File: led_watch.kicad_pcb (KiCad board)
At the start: 6 copper layers, 29 x 29 mm, 107 parts, among them U3 M0G3507QDGS32RQ1, Y2 TXC-7C

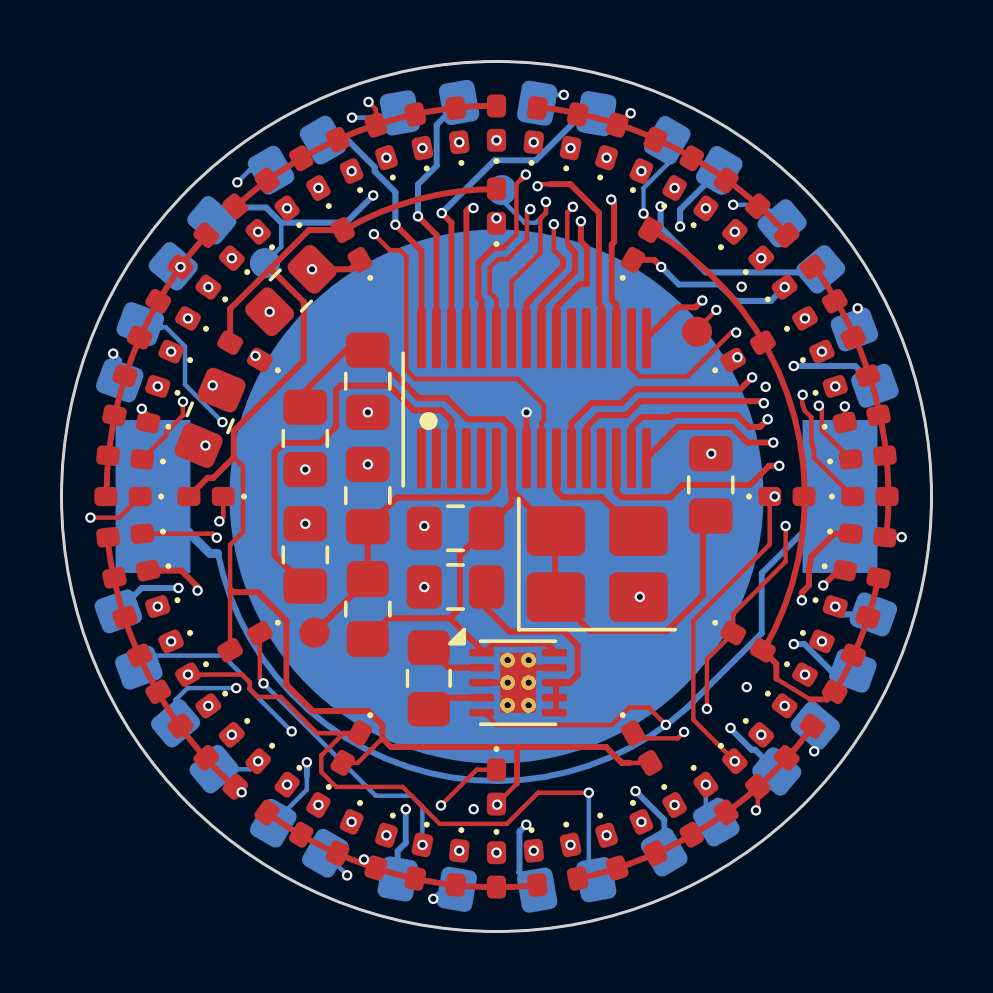
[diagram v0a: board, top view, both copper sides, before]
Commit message: 4 layers, removed regulator
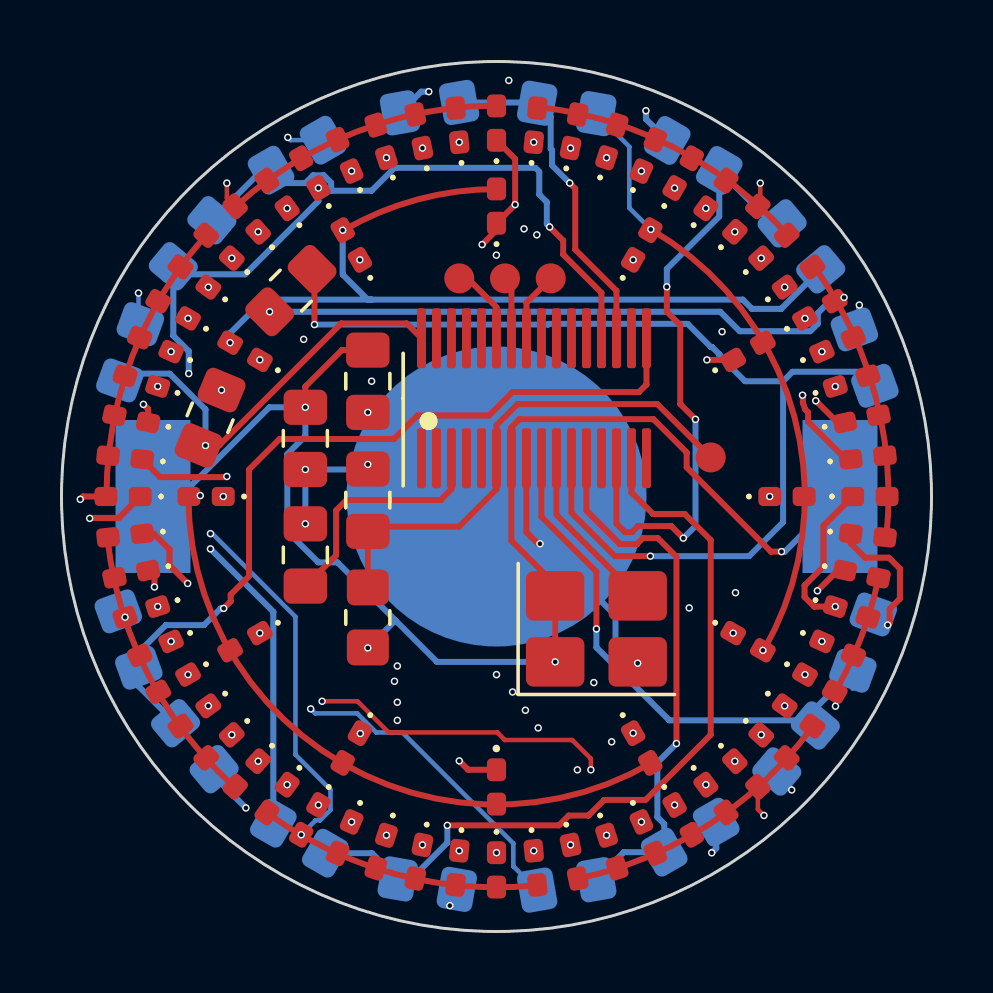
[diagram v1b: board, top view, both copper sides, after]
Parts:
- removed C1, C2: 10uF, Capacitor_SMD:C_0805_2012Metric_Pad1.18x1.45mm_HandSolder
- removed C3: 0.1uF, Capacitor_SMD:C_0805_2012Metric_Pad1.18x1.45mm_HandSolder
- removed L1: 2.2uH, Inductor_SMD:L_0805_2012Metric_Pad1.15x1.40mm_HandSolder
- removed PS1: TPS63031DSKR, Package_SON:WSON-10-1EP_2.5x2.5mm_P0.5mm_EP1.2x2mm_ThermalVias
- TP3, TP6: moved to F.Cu
- moved TP5 14.4 mm to (114.3, 50.9)
- moved TP6 9.54 mm to (109.0, 45.0)
- moved TP4 8.12 mm to (105.9, 45.0)
- moved TP3 2.94 mm to (107.4, 45.0)
- moved Y2 2.16 mm to (110.5, 56.6)
- moved R19 0.28 mm to (102.9, 56.3)
- moved C4 0.15 mm to (102.9, 52.3)
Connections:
- C7 pad 1: +3V3 -> +VBATT
- C8 pad 1: +3V3 -> +VBATT
- R10 pad 1: PA9 -> Net-(D33-A)
- R10 pad 2: Net-(D1-A) -> PA10
- R11 pad 1: PA16/SPI1_POCI -> PA25/SPI1_CS3
- R11 pad 2: Net-(D10-A) -> Net-(D13-K)
- R12 pad 1: PA17/SPI1_CLK -> Net-(D41-A)
- R12 pad 2: Net-(D17-A) -> PA25/SPI1_CS3
- R13 pad 1: PA18/SPI1_PICO/BSL_Invoke -> PA13/TFT_D/C
- R13 pad 2: Net-(D25-A) -> Net-(D14-K)
- R14 pad 1: PA25/SPI1_CS3 -> Net-(D49-A)
- R14 pad 2: Net-(D33-A) -> PA13/TFT_D/C
- R15 pad 1: PA24/TFT_RESET -> PA12
- R15 pad 2: Net-(D41-A) -> Net-(D15-K)
- R16 pad 1: PA23 -> Net-(D57-A)
- R16 pad 2: Net-(D49-A) -> PA12
- R17 pad 1: PA22 -> PA7
- R17 pad 2: Net-(D57-A) -> Net-(D16-K)
- R18 pad 1: PA21 -> Net-(D65-A)
- R18 pad 2: Net-(D65-A) -> PA7
- R19 pad 1: +3V3 -> +VBATT
- R2 pad 1: PA2 -> Net-(D1-A)
- R2 pad 2: Net-(D1-K) -> PA4
- R3 pad 1: PA5/HFXIN -> PA2
- R3 pad 2: Net-(D10-K) -> Net-(D1-K)
- R4 pad 1: PA8/SPI0_CS0 -> Net-(D10-A)
- R4 pad 2: Net-(D11-K) -> PA2
- R5 pad 1: PA10 -> PA5/HFXIN
- R5 pad 2: Net-(D12-K) -> Net-(D10-K)
- R6 pad 1: PA11/SPI0_SCK -> Net-(D17-A)
- R6 pad 2: Net-(D13-K) -> PA5/HFXIN
- R7 pad 1: PA12 -> PA8/SPI0_CS0
- R7 pad 2: Net-(D14-K) -> Net-(D11-K)
- R8 pad 1: PA13/TFT_D/C -> Net-(D25-A)
- R8 pad 2: Net-(D15-K) -> PA8/SPI0_CS0
- R9 pad 1: PA7 -> PA10
- R9 pad 2: Net-(D16-K) -> Net-(D12-K)
- U3 pad 7: +3V3 -> +VBATT
- Y2 pad 1: +3V3 -> +VBATT
- Y2 pad 4: +3V3 -> +VBATT
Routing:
- net Net-(D65-A): track 88.9 -> 30.9 mm, vias 2 -> 3
- net +3V3: track 36.6 -> 0.00 mm
- net PA11/SPI0_SCK: track 34.8 -> 0.00 mm, vias 2 -> 0
- net PA12: track 42.8 -> 11.5 mm, vias 2 -> 1
- net PA9: track 29.0 -> 0.00 mm, vias 2 -> 0
- net +VBATT: track 20.8 -> 48.4 mm, vias 1 -> 4
- net PA13/TFT_D/C: track 46.1 -> 19.1 mm, vias 2 -> 1
- net PA17/SPI1_CLK: track 26.9 -> 0.00 mm, vias 2 -> 0
- net PA16/SPI1_POCI: track 26.4 -> 0.00 mm, vias 2 -> 0
- net Net-(D33-A): track 24.8 -> 0.00 mm, vias 2 -> 1
- net PA4: track 12.3 -> 36.3 mm
- net PA18/SPI1_PICO/BSL_Invoke: track 24.5 -> 2.33 mm, vias 2 -> 0
- net Net-(D17-K): track 101.5 -> 81.0 mm, vias 9 -> 12
- net PA21: track 19.5 -> 0.00 mm, vias 2 -> 0
- net PA22: track 17.6 -> 0.00 mm, vias 2 -> 0
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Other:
- copper layers 6 -> 4

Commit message: remove half of resistors, routing cleanup
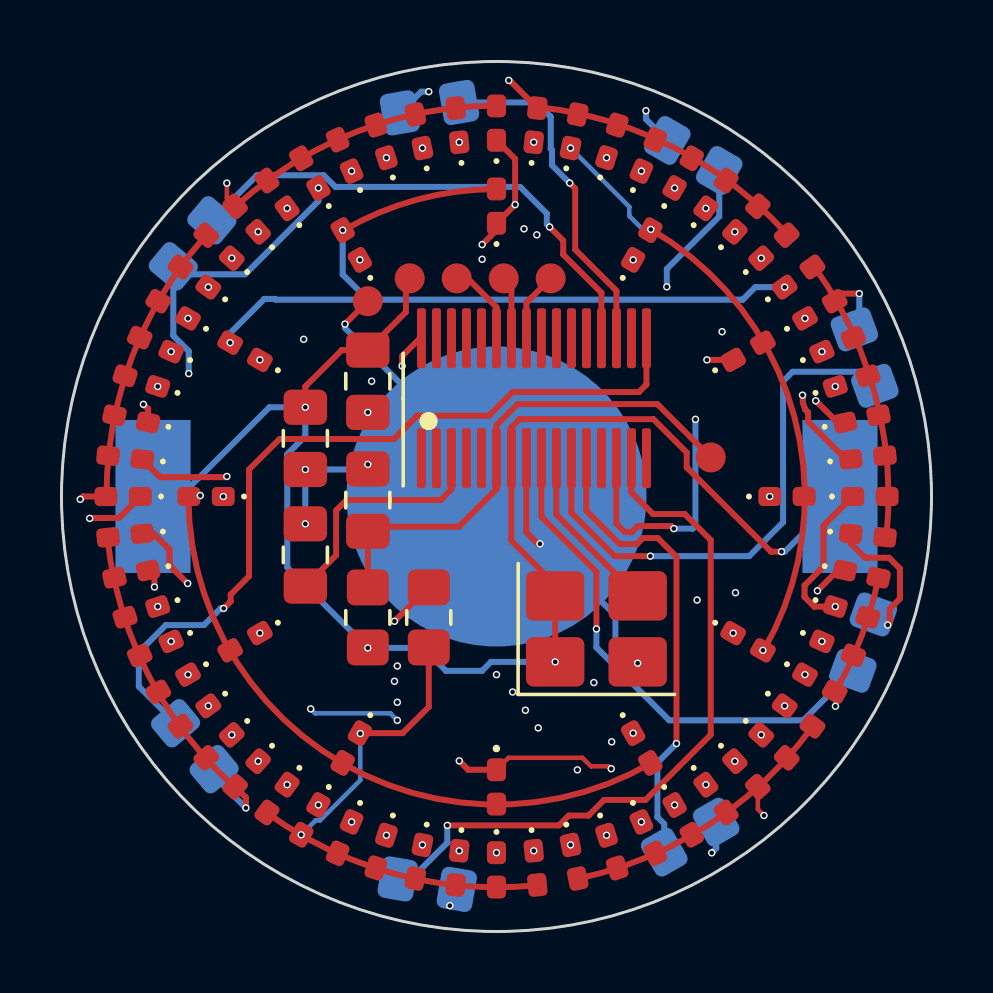
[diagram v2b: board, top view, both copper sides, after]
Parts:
- removed R10, R12, R14, R16, R18, R2, R4, R6, R8: 75, Resistor_SMD:R_0805_2012Metric_Pad1.20x1.40mm_HandSolder
- added TP1: TestPoint, TestPoint:TestPoint_Pad_D1.0mm, F.Cu at (104.3, 45.0)
- added TP2: TestPoint, TestPoint:TestPoint_Pad_D1.0mm, F.Cu at (102.9, 45.7)
- moved R11 9.87 mm to (104.9, 56.3), turned to -90 degrees
- moved TP4 0.08 mm to (105.8, 45.0)
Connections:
- D1 pad 1: Net-(D1-K) -> PA2
- D1 pad 2: Net-(D1-A) -> PA4
- D10 pad 1: Net-(D10-K) -> PA5/HFXIN
- D10 pad 2: Net-(D10-A) -> PA2
- D11 pad 1: Net-(D11-K) -> PA8/SPI0_CS0
- D11 pad 2: Net-(D10-A) -> PA2
- D12 pad 1: Net-(D12-K) -> PA10
- D12 pad 2: Net-(D10-A) -> PA2
- D13 pad 1: Net-(D13-K) -> PA25/SPI1_CS3
- D13 pad 2: Net-(D10-A) -> PA2
- D14 pad 1: Net-(D14-K) -> PA13/TFT_D/C
- D14 pad 2: Net-(D10-A) -> PA2
- D15 pad 1: Net-(D15-K) -> PA12
- D15 pad 2: Net-(D10-A) -> PA2
- D16 pad 1: Net-(D16-K) -> PA7
- D16 pad 2: Net-(D10-A) -> PA2
- D17 pad 1: Net-(D17-K) -> PA4
- D17 pad 2: Net-(D17-A) -> PA5/HFXIN
- D18 pad 1: Net-(D1-K) -> PA2
- D18 pad 2: Net-(D17-A) -> PA5/HFXIN
- D19 pad 1: Net-(D11-K) -> PA8/SPI0_CS0
- D19 pad 2: Net-(D17-A) -> PA5/HFXIN
- D2 pad 1: Net-(D10-K) -> PA5/HFXIN
- D2 pad 2: Net-(D1-A) -> PA4
- D20 pad 1: Net-(D12-K) -> PA10
- D20 pad 2: Net-(D17-A) -> PA5/HFXIN
- D21 pad 1: Net-(D13-K) -> PA25/SPI1_CS3
- D21 pad 2: Net-(D17-A) -> PA5/HFXIN
- D22 pad 1: Net-(D14-K) -> PA13/TFT_D/C
- D22 pad 2: Net-(D17-A) -> PA5/HFXIN
- D23 pad 1: Net-(D15-K) -> PA12
- D23 pad 2: Net-(D17-A) -> PA5/HFXIN
- D24 pad 1: Net-(D16-K) -> PA7
- D24 pad 2: Net-(D17-A) -> PA5/HFXIN
- D25 pad 1: Net-(D17-K) -> PA4
- D25 pad 2: Net-(D25-A) -> PA8/SPI0_CS0
- D26 pad 1: Net-(D1-K) -> PA2
- D26 pad 2: Net-(D25-A) -> PA8/SPI0_CS0
- D27 pad 1: Net-(D10-K) -> PA5/HFXIN
- D27 pad 2: Net-(D25-A) -> PA8/SPI0_CS0
- D28 pad 1: Net-(D12-K) -> PA10
- D28 pad 2: Net-(D25-A) -> PA8/SPI0_CS0
- D29 pad 1: Net-(D13-K) -> PA25/SPI1_CS3
- D29 pad 2: Net-(D25-A) -> PA8/SPI0_CS0
- D3 pad 1: Net-(D11-K) -> PA8/SPI0_CS0
- D3 pad 2: Net-(D1-A) -> PA4
- D30 pad 1: Net-(D14-K) -> PA13/TFT_D/C
- D30 pad 2: Net-(D25-A) -> PA8/SPI0_CS0
- D31 pad 1: Net-(D15-K) -> PA12
- D31 pad 2: Net-(D25-A) -> PA8/SPI0_CS0
- D32 pad 1: Net-(D16-K) -> PA7
- D32 pad 2: Net-(D25-A) -> PA8/SPI0_CS0
- D33 pad 1: Net-(D17-K) -> PA4
- D33 pad 2: Net-(D33-A) -> PA10
- D34 pad 1: Net-(D1-K) -> PA2
- D34 pad 2: Net-(D33-A) -> PA10
- D35 pad 1: Net-(D10-K) -> PA5/HFXIN
- D35 pad 2: Net-(D33-A) -> PA10
- D36 pad 1: Net-(D11-K) -> PA8/SPI0_CS0
- D36 pad 2: Net-(D33-A) -> PA10
- D37 pad 1: Net-(D13-K) -> PA25/SPI1_CS3
- D37 pad 2: Net-(D33-A) -> PA10
- D38 pad 1: Net-(D14-K) -> PA13/TFT_D/C
- D38 pad 2: Net-(D33-A) -> PA10
- D39 pad 1: Net-(D15-K) -> PA12
- D39 pad 2: Net-(D33-A) -> PA10
- D4 pad 1: Net-(D12-K) -> PA10
- D4 pad 2: Net-(D1-A) -> PA4
- D40 pad 1: Net-(D16-K) -> PA7
- D40 pad 2: Net-(D33-A) -> PA10
- D41 pad 1: Net-(D17-K) -> PA4
- D41 pad 2: Net-(D41-A) -> PA25/SPI1_CS3
- D42 pad 1: Net-(D1-K) -> PA2
- D42 pad 2: Net-(D41-A) -> PA25/SPI1_CS3
- D43 pad 1: Net-(D10-K) -> PA5/HFXIN
- D43 pad 2: Net-(D41-A) -> PA25/SPI1_CS3
- D44 pad 1: Net-(D11-K) -> PA8/SPI0_CS0
- D44 pad 2: Net-(D41-A) -> PA25/SPI1_CS3
- D45 pad 1: Net-(D12-K) -> PA10
- D45 pad 2: Net-(D41-A) -> PA25/SPI1_CS3
- D46 pad 1: Net-(D14-K) -> PA13/TFT_D/C
- D46 pad 2: Net-(D41-A) -> PA25/SPI1_CS3
- D47 pad 1: Net-(D15-K) -> PA12
- D47 pad 2: Net-(D41-A) -> PA25/SPI1_CS3
- D48 pad 1: Net-(D16-K) -> PA7
- D48 pad 2: Net-(D41-A) -> PA25/SPI1_CS3
- D49 pad 1: Net-(D17-K) -> PA4
- D49 pad 2: Net-(D49-A) -> PA13/TFT_D/C
- D5 pad 1: Net-(D13-K) -> PA25/SPI1_CS3
- D5 pad 2: Net-(D1-A) -> PA4
- D50 pad 1: Net-(D1-K) -> PA2
- D50 pad 2: Net-(D49-A) -> PA13/TFT_D/C
- D51 pad 1: Net-(D10-K) -> PA5/HFXIN
- D51 pad 2: Net-(D49-A) -> PA13/TFT_D/C
- D52 pad 1: Net-(D11-K) -> PA8/SPI0_CS0
- D52 pad 2: Net-(D49-A) -> PA13/TFT_D/C
- D53 pad 1: Net-(D12-K) -> PA10
- D53 pad 2: Net-(D49-A) -> PA13/TFT_D/C
- D54 pad 1: Net-(D13-K) -> PA25/SPI1_CS3
- D54 pad 2: Net-(D49-A) -> PA13/TFT_D/C
- D55 pad 1: Net-(D15-K) -> PA12
- D55 pad 2: Net-(D49-A) -> PA13/TFT_D/C
- D56 pad 1: Net-(D16-K) -> PA7
- D56 pad 2: Net-(D49-A) -> PA13/TFT_D/C
- D57 pad 1: Net-(D17-K) -> PA4
- D57 pad 2: Net-(D57-A) -> PA12
- D58 pad 1: Net-(D1-K) -> PA2
- D58 pad 2: Net-(D57-A) -> PA12
- D59 pad 1: Net-(D10-K) -> PA5/HFXIN
- D59 pad 2: Net-(D57-A) -> PA12
- D6 pad 1: Net-(D14-K) -> PA13/TFT_D/C
- D6 pad 2: Net-(D1-A) -> PA4
- D60 pad 1: Net-(D11-K) -> PA8/SPI0_CS0
- D60 pad 2: Net-(D57-A) -> PA12
- D61 pad 1: Net-(D12-K) -> PA10
- D61 pad 2: Net-(D57-A) -> PA12
- D62 pad 1: Net-(D13-K) -> PA25/SPI1_CS3
- D62 pad 2: Net-(D57-A) -> PA12
- D63 pad 1: Net-(D14-K) -> PA13/TFT_D/C
- D63 pad 2: Net-(D57-A) -> PA12
- D64 pad 1: Net-(D16-K) -> PA7
- D64 pad 2: Net-(D57-A) -> PA12
- D65 pad 1: Net-(D17-K) -> PA4
- D65 pad 2: Net-(D65-A) -> PA7
- D66 pad 1: Net-(D1-K) -> PA2
- D66 pad 2: Net-(D65-A) -> PA7
- D67 pad 1: Net-(D10-K) -> PA5/HFXIN
- D67 pad 2: Net-(D65-A) -> PA7
- D68 pad 1: Net-(D11-K) -> PA8/SPI0_CS0
- D68 pad 2: Net-(D65-A) -> PA7
- D69 pad 1: Net-(D12-K) -> PA10
- D69 pad 2: Net-(D65-A) -> PA7
- D7 pad 1: Net-(D15-K) -> PA12
- D7 pad 2: Net-(D1-A) -> PA4
- D70 pad 1: Net-(D13-K) -> PA25/SPI1_CS3
- D70 pad 2: Net-(D65-A) -> PA7
- D71 pad 1: Net-(D14-K) -> PA13/TFT_D/C
- D71 pad 2: Net-(D65-A) -> PA7
- D72 pad 1: Net-(D15-K) -> PA12
- D72 pad 2: Net-(D65-A) -> PA7
- D8 pad 1: Net-(D16-K) -> PA7
- D8 pad 2: Net-(D1-A) -> PA4
- D9 pad 1: Net-(D17-K) -> PA4
- D9 pad 2: Net-(D10-A) -> PA2
- R1 pad 1: PA4 -> Net-(U3-PA4/LFCLK_IN/LFXOUT)
- R1 pad 2: Net-(D17-K) -> PA4
- R11 pad 1: PA25/SPI1_CS3 -> Net-(U3-PA25/A0_2)
- R11 pad 2: Net-(D13-K) -> PA25/SPI1_CS3
- R13 pad 1: PA13/TFT_D/C -> Net-(U3-PA13)
- R13 pad 2: Net-(D14-K) -> PA13/TFT_D/C
- R15 pad 1: PA12 -> Net-(U3-PA12/FCC_IN)
- R15 pad 2: Net-(D15-K) -> PA12
- R17 pad 1: PA7 -> Net-(U3-PA7/CLK_OUT)
- R17 pad 2: Net-(D16-K) -> PA7
- R3 pad 1: PA2 -> Net-(U3-PA2/ROSC)
- R3 pad 2: Net-(D1-K) -> PA2
- R5 pad 1: PA5/HFXIN -> Net-(U3-PA5/HFXIN/FCC_IN)
- R5 pad 2: Net-(D10-K) -> PA5/HFXIN
- R7 pad 1: PA8/SPI0_CS0 -> Net-(U3-PA8)
- R7 pad 2: Net-(D11-K) -> PA8/SPI0_CS0
- R9 pad 1: PA10 -> Net-(U3-PA10/CLK_OUT)
- R9 pad 2: Net-(D12-K) -> PA10
- U3 pad 1: PA26 -> unconnected-(U3-PA26/A0_1-Pad1)
- U3 pad 11: PA4 -> Net-(U3-PA4/LFCLK_IN/LFXOUT)
- U3 pad 12: PA5/HFXIN -> Net-(U3-PA5/HFXIN/FCC_IN)
- U3 pad 13: PA6/HFXOUT -> unconnected-(U3-PA6/HFCLK_IN/HFXOUT-Pad13)
- U3 pad 14: PA7 -> Net-(U3-PA7/CLK_OUT)
- U3 pad 15: PA8/SPI0_CS0 -> Net-(U3-PA8)
- U3 pad 16: PA9 -> unconnected-(U3-PA9/RTC_OUT/CLK_OUT-Pad16)
- U3 pad 17: PA10 -> Net-(U3-PA10/CLK_OUT)
- U3 pad 18: PA11/SPI0_SCK -> unconnected-(U3-PA11-Pad18)
- U3 pad 19: PA12 -> Net-(U3-PA12/FCC_IN)
- U3 pad 2: PA27/SPI1_CS1 -> unconnected-(U3-PA27/RTC_OUT/A0_0-Pad2)
- U3 pad 20: PA13/TFT_D/C -> Net-(U3-PA13)
- U3 pad 21: PA14/SPI0_PICO -> unconnected-(U3-PA14/CLK_OUT/A0_12-Pad21)
- U3 pad 22: PA15/DACOUT -> unconnected-(U3-PA15/A1_0/DACOUT-Pad22)
- U3 pad 23: PA16/SPI1_POCI -> unconnected-(U3-PA16/A1_1/FCC_IN-Pad23)
- U3 pad 24: PA17/SPI1_CLK -> unconnected-(U3-PA17/A1_2-Pad24)
- U3 pad 28: PA21 -> unconnected-(U3-PA21/A1_7/VREF--Pad28)
- U3 pad 29: PA22 -> unconnected-(U3-PA22/CLK_OUT/A0_7-Pad29)
- U3 pad 30: PA23 -> unconnected-(U3-PA23/VREF+-Pad30)
- U3 pad 31: PA24/TFT_RESET -> unconnected-(U3-PA24/A0_3-Pad31)
- U3 pad 32: PA25/SPI1_CS3 -> Net-(U3-PA25/A0_2)
- U3 pad 4: PA0 -> unconnected-(U3-PA0-Pad4)
- U3 pad 5: PA1 -> unconnected-(U3-PA1-Pad5)
- U3 pad 9: PA2 -> Net-(U3-PA2/ROSC)
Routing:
- net PA5/HFXIN: track 18.4 -> 111.6 mm, vias 1 -> 13
- net PA7: track 21.1 -> 112.7 mm, vias 3 -> 15
- net Net-(D10-K): track 89.2 -> 0.00 mm, vias 11 -> 0
- net Net-(D16-K): track 83.5 -> 0.00 mm, vias 12 -> 0
- net Net-(D15-K): track 82.7 -> 0.00 mm, vias 12 -> 0
- net Net-(D1-K): track 81.9 -> 0.00 mm, vias 12 -> 0
- net Net-(D11-K): track 81.4 -> 0.00 mm, vias 10 -> 0
- net Net-(D12-K): track 81.3 -> 0.00 mm, vias 11 -> 0
- net Net-(D17-K): track 81.0 -> 0.00 mm, vias 12 -> 0
- net PA12: track 11.5 -> 91.5 mm, vias 1 -> 15
- net Net-(D13-K): track 69.9 -> 0.00 mm, vias 11 -> 0
- net PA25/SPI1_CS3: track 13.7 -> 78.8 mm, vias 1 -> 11
- net PA2: track 18.4 -> 83.3 mm, vias 1 -> 12
- net Net-(D14-K): track 64.5 -> 0.00 mm, vias 9 -> 0
- net PA8/SPI0_CS0: track 26.5 -> 87.7 mm, vias 1 -> 11
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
